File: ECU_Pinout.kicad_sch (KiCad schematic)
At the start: 2 parts

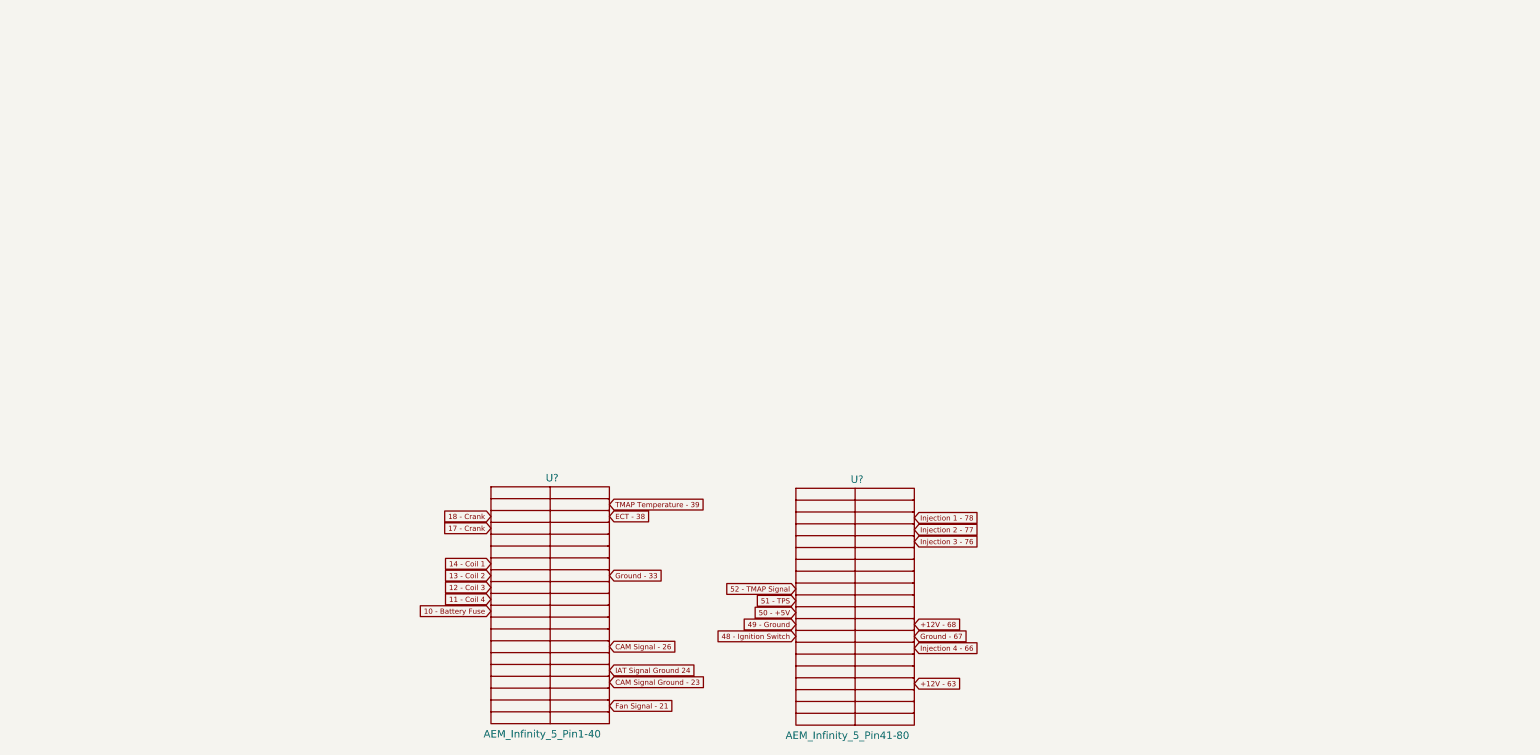
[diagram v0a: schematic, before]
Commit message: Infinity 5 and 7 Pinouts
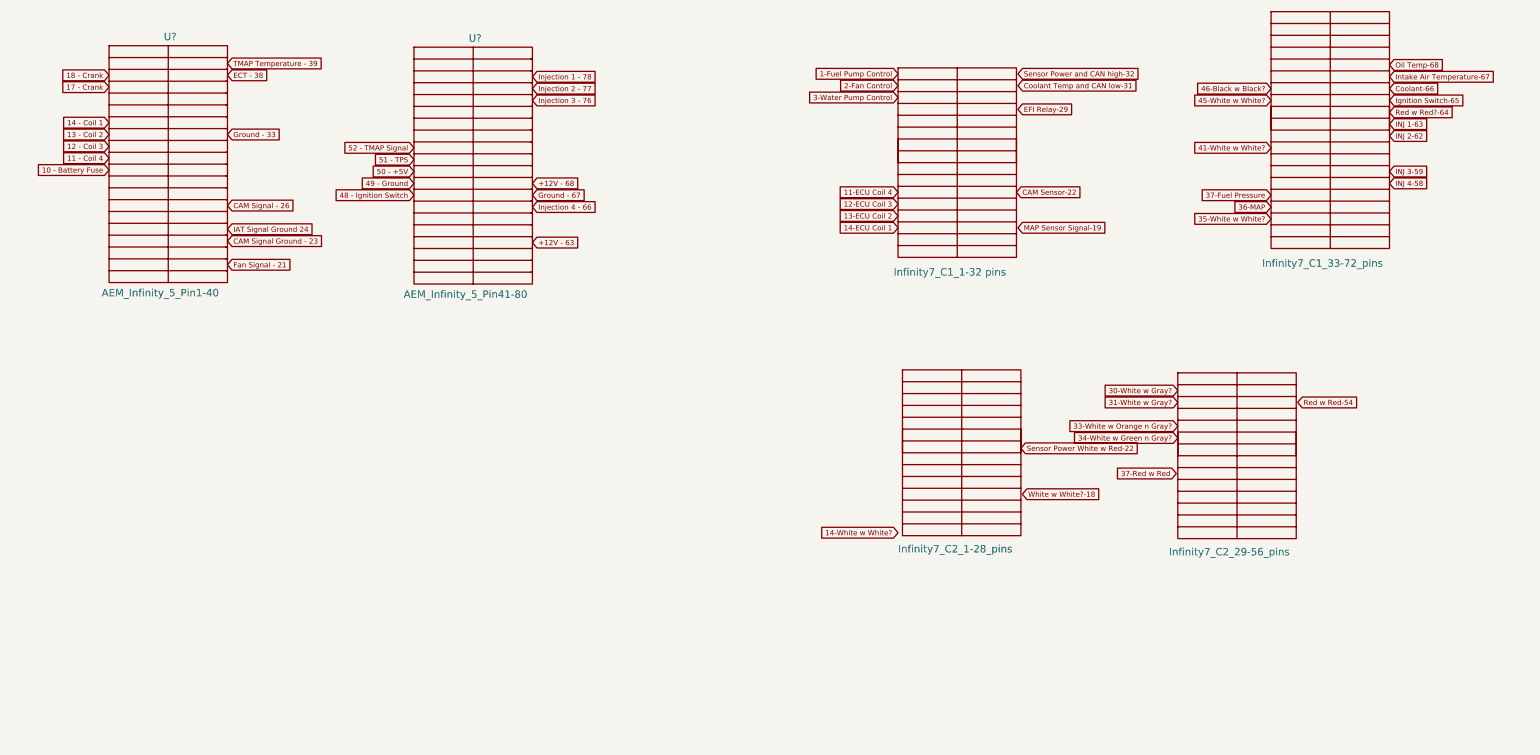
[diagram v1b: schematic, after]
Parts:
- added U?: Infinity7_C2_29-56_pins, symbol Ty lib:Infinity7_C2_29-56_pins
- added U?: Infinity7_C1_33-72_pins, symbol Ty lib:Infinity7_C1_33-72_pins
- added U?: Infinity7_C2_1-28_pins, symbol Ty lib:Infinity7_C2_1-28_pins
- added U?: Infinity7_C1_1-32 pins, symbol Ty lib:Infinity7_C1_1-32 pins
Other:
- moved on the sheet: U?

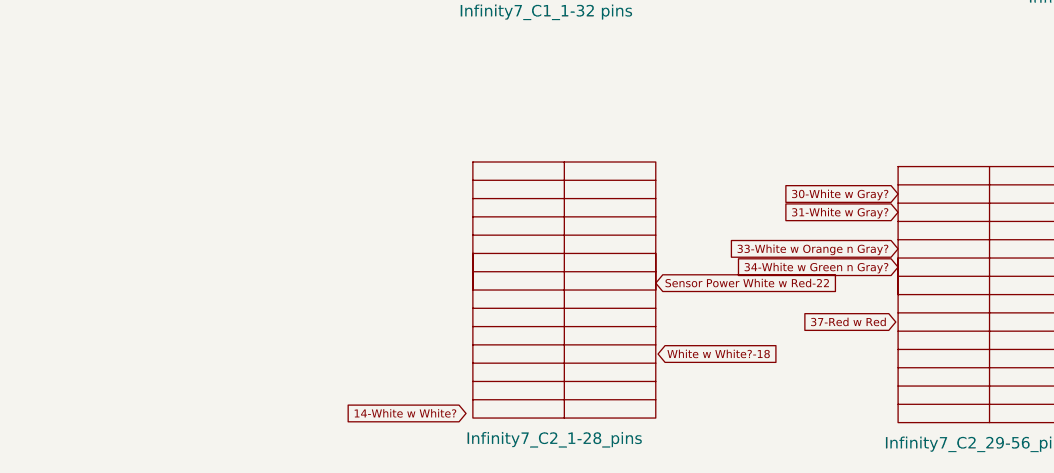
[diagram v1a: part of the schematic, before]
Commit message: Updated Connectors
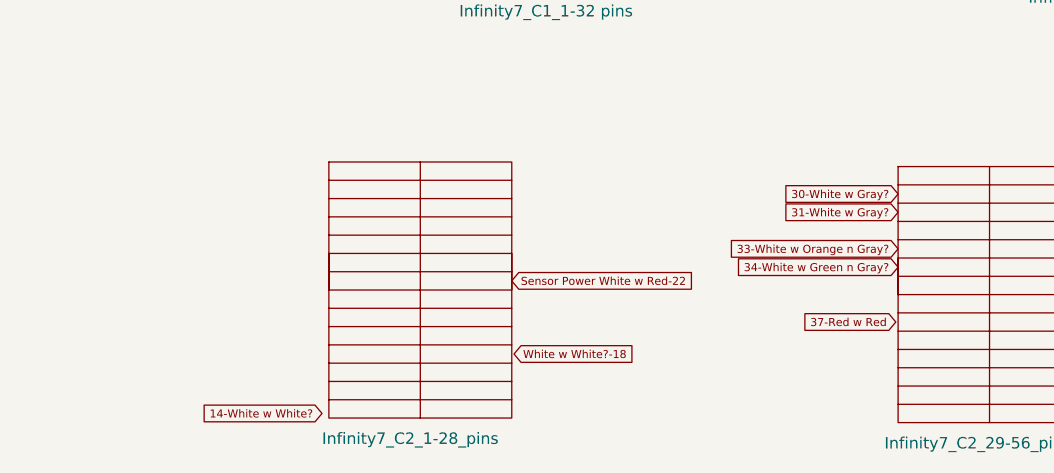
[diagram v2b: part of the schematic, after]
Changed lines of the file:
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@@
     )
   )
-  (global_label "Sensor Power White w Red-22" (shape input) (at 198.374 96.266 0) (fields_autoplaced)
-    (effects (font (size 0.889 0.889)) (justify left))
-    (property "Intersheet References" "${INTERSHEET_REFS}" (id 0) (at 220.8911 96.2105 0)
+  (global_label "Sensor Power White w Red-22" (shape input) (at 182.372 96.012 0) (fields_autoplaced)
+    (effects (font (size 0.889 0.889)) (justify left))
+    (property "Intersheet References" "${INTERSHEET_REFS}" (id 0) (at 204.8891 95.9565 0)
       (effects (font (size 0.889 0.889)) (justify left) hide)
     )
@@
     )
   )
-  (global_label "White w White?-18" (shape input) (at 198.628 104.14 0) (fields_autoplaced)
-    (effects (font (size 0.889 0.889)) (justify left))
-    (property "Intersheet References" "${INTERSHEET_REFS}" (id 0) (at 213.1864 104.0845 0)
+  (global_label "White w White?-18" (shape input) (at 182.626 104.14 0) (fields_autoplaced)
+    (effects (font (size 0.889 0.889)) (justify left))
+    (property "Intersheet References" "${INTERSHEET_REFS}" (id 0) (at 197.1844 104.0845 0)
       (effects (font (size 0.889 0.889)) (justify left) hide)
     )
@@
     )
   )
-  (global_label "14-White w White?" (shape input) (at 177.292 110.744 180) (fields_autoplaced)
-    (effects (font (size 0.889 0.889)) (justify right))
-    (property "Intersheet References" "${INTERSHEET_REFS}" (id 0) (at 162.7336 110.6885 0)
+  (global_label "14-White w White?" (shape input) (at 161.29 110.744 180) (fields_autoplaced)
+    (effects (font (size 0.889 0.889)) (justify right))
+    (property "Intersheet References" "${INTERSHEET_REFS}" (id 0) (at 146.7316 110.6885 0)
       (effects (font (size 0.889 0.889)) (justify right) hide)
     )
@@
     )
   )
-  (symbol (lib_id "Ty lib:Infinity7_C2_1-28_pins") (at 188.214 97.028 0) (unit 1)
+  (symbol (lib_id "Ty lib:Infinity7_C2_1-28_pins") (at 172.212 97.028 0) (unit 1)
     (in_bom yes) (on_board yes)
-    (property "Reference" "U?" (id 0) (at 188.214 78.994 0)
-      (effects (font (size 1.27 1.27)) hide)
-    )
-    (property "Value" "Infinity7_C2_1-28_pins" (id 1) (at 177.292 113.538 0)
-      (effects (font (size 1.27 1.27)) (justify left))
-    )
-    (property "Footprint" "" (id 2) (at 188.214 97.028 0)
-      (effects (font (size 1.27 1.27)) hide)
-    )
-    (property "Datasheet" "" (id 3) (at 188.214 97.028 0)
-      (effects (font (size 1.27 1.27)) hide)
-    )
+    (property "Reference" "U?" (id 0) (at 172.212 78.994 0)
+      (effects (font (size 1.27 1.27)) hide)
+    )
+    (property "Value" "Infinity7_C2_1-28_pins" (id 1) (at 161.29 113.538 0)
+      (effects (font (size 1.27 1.27)) (justify left))
+    )
+    (property "Footprint" "" (id 2) (at 172.212 97.028 0)
+      (effects (font (size 1.27 1.27)) hide)
+    )
+    (property "Datasheet" "" (id 3) (at 172.212 97.028 0)
+      (effects (font (size 1.27 1.27)) hide)
+    )
